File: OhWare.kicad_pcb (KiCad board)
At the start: 2 copper layers, 100 x 100 mm, 107 parts, among them J1 Screw_Terminal_01x03, J10 Conn_02x15_Odd_Even, J11 Conn_01x04_Pin, J12 Conn_01x03_Pin, J15 RJ45_Hanrun_HR911105A_Horizon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, J2 Conn_01x04_Pin, J4 Conn_01x02_Pin, J5 Conn_01x04_Pin, J6 Conn_01x02_Pin, J7 Conn_01x06_Pin, J8 Conn_01x04_Pin, J9 Conn_02x10_Odd_Even, SW1 SW_DIP_x01, SW2 SW_DIP_x01, SW3 SW_DIP_x01, U1 STM32F407VETx, U10 SP3485EN-L/TR, U2 SIT65HVD230DR, U3 SIT3490EESA, U4 XL1509-5.0E1, U5 AMS1117-3.3, U6 TL431M-0.3%-6AF, U7 LAN8720AI-CP-TR, U8 USB-TYPE-C-016, X1 X32258MOB4SI, X2 ABS07-32.768KHZ-T, X3 XL2EL89CSI-111YLC-25M

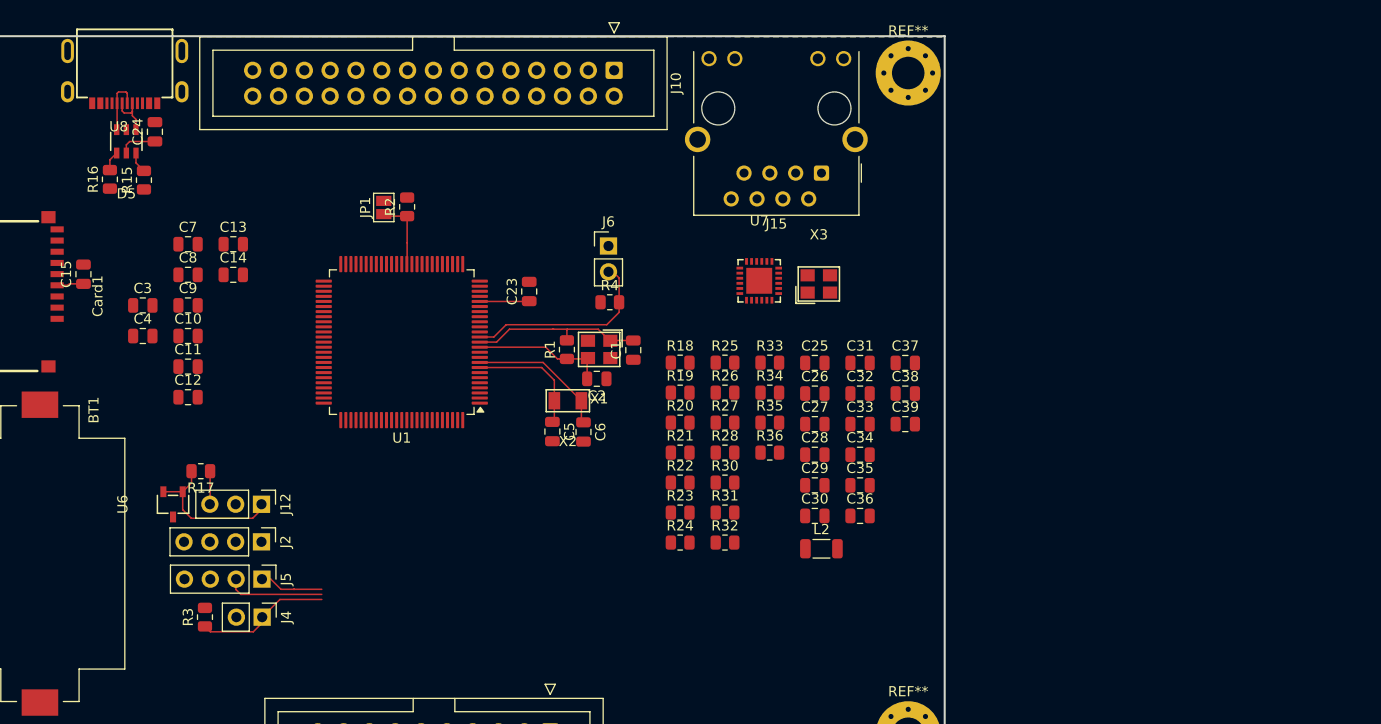
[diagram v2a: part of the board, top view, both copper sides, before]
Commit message: mcu circuit Done , + Ehernet Done (still placement is negotiable (best placement for minimal routing hustle))
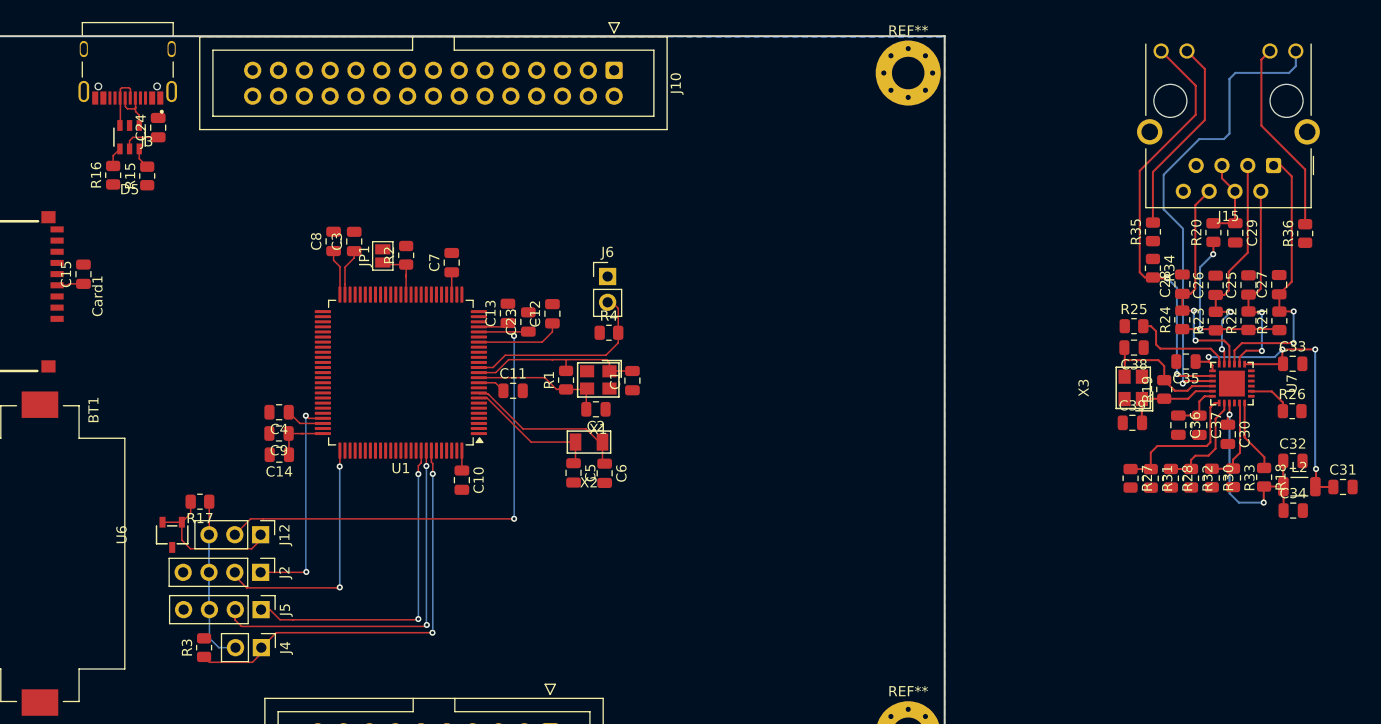
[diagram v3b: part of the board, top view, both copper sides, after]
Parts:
- removed U8: USB-TYPE-C-016, EasyEDA:USB-SMD_TYPE-C16PCB1.6073
- added J3: CQ-USB-C16PSMT01, EasyEDA:SHENZHEN-CHUANGQIN-TECHNOLOGY_CQ-USB-C16PSMT01, F.Cu at (119.6, 56.1)
- moved R21 60.4 mm to (232.9, 78.0), turned to 90 degrees
- moved R18 58.5 mm to (231.4, 93.4), turned to -90 degrees
- moved R22 58.1 mm to (229.9, 78.0), turned to 90 degrees
- moved R36 56.9 mm to (235.5, 69.4), turned to 90 degrees
- moved R23 56.0 mm to (226.7, 78.0), turned to 90 degrees
- moved R26 55.8 mm to (234.2, 86.9)
- moved R20 55.7 mm to (226.4, 69.3), turned to 90 degrees
- moved R24 54.0 mm to (223.4, 77.9), turned to 90 degrees
- moved C31 49.1 mm to (239.2, 94.4)
- moved C29 48.2 mm to (228.6, 69.4), turned to -90 degrees
- moved R30 47.9 mm to (226.3, 93.5), turned to -90 degrees
- moved C27 47.7 mm to (232.9, 74.5), turned to 90 degrees
- moved R19 47.6 mm to (221.6, 84.8), turned to 90 degrees
- moved U7 47.6 mm to (228.3, 84.2), turned to -90 degrees
- moved L2 47.4 mm to (234.9, 94.3)
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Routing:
- net +3V3: track 5.91 -> 70.1 mm, vias 0 -> 2
- net /Controller/VREF: track 4.88 -> 51.4 mm, vias 0 -> 2
- net /Ethernet/LED1/REGOFF: track 0.00 -> 46.4 mm, vias 0 -> 1
- net /Ethernet/LED2/nINTSEL: track 0.00 -> 41.8 mm, vias 0 -> 2
- net /Ethernet/VDDA: track 0.00 -> 34.1 mm, vias 0 -> 4
- net /Controller/BOOT0: track 13.4 -> 42.2 mm, vias 0 -> 2
- net /Ethernet/TXP: track 0.00 -> 28.1 mm, vias 0 -> 2
- net /Controller/UART1_Rx: track 9.94 -> 37.6 mm, vias 0 -> 2
- net /Controller/UART1_Tx: track 6.36 -> 32.7 mm, vias 0 -> 2
- net /Controller/SWCLK (PA14): track 0.00 -> 24.7 mm, vias 0 -> 2
- net /Ethernet/RXP: track 0.00 -> 23.3 mm, vias 0 -> 2
- net /Ethernet/RXN: track 0.00 -> 22.8 mm, vias 0 -> 2
- net /Controller/SWDIO (PA13): track 0.00 -> 21.7 mm, vias 0 -> 2
- net /Ethernet/TXN: track 0.00 -> 21.0 mm, vias 0 -> 2
- net Net-(J15-Pad11): track 0.00 -> 19.7 mm
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
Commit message: Added Base
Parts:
- removed BT1: CR2032, Battery:BatteryHolder_Keystone_1060_1x2032
- removed C10, C11, C12, C13, C15, C23, C24, C7, C8, C9: 100n, Capacitor_SMD:C_0805_2012Metric
- removed C14, C31, C32: 4.7u, Capacitor_SMD:C_0805_2012Metric
- removed C25, C26, C27, C28: 10pF, Capacitor_SMD:C_0805_2012Metric
- removed C29: 22nF, Capacitor_SMD:C_0805_2012Metric
- removed C3, C4: 2.2u, Capacitor_SMD:C_0805_2012Metric
- removed C30, C33, C34, C35, C37: 0.1uF, Capacitor_SMD:C_0805_2012Metric
- removed C36: 1uF, Capacitor_SMD:C_0805_2012Metric
- removed C38, C39: 30pF, Capacitor_SMD:C_0805_2012Metric
- removed C5, C6: 12.5pF, Capacitor_SMD:C_0805_2012Metric
- removed Card1: TF-01A, EasyEDA:TF-SMD_TF-01A
- removed D5: USBLC6-2SC6, EasyEDA:SOT-23-6_L2.9-W1.6-P0.95-LS2.8-BL
- removed J12: Conn_01x03_Pin, Connector_PinHeader_2.54mm:PinHeader_1x03_P2.54mm_Vertical
- removed J15: RJ45_Hanrun_HR911105A_Horizontal, EasyEDA:RJ45_Hanrun_HR911105A_Horizontal
- removed J2, J5: Conn_01x04_Pin, Connector_PinHeader_2.54mm:PinHeader_1x04_P2.54mm_Vertical
- removed J3: CQ-USB-C16PSMT01, EasyEDA:SHENZHEN-CHUANGQIN-TECHNOLOGY_CQ-USB-C16PSMT01
- removed J4, J6: Conn_01x02_Pin, Connector_PinHeader_2.54mm:PinHeader_1x02_P2.54mm_Vertical
- removed JP1: Jumper_2_Open, Jumper:SolderJumper-2_P1.3mm_Open_Pad1.0x1.5mm
- removed L2: 2A/0.05, Inductor_SMD:L_1206_3216Metric
- removed R1, R2, R3, R4: 10K, Resistor_SMD:R_0805_2012Metric
- removed R15, R16, R20: 0, Resistor_SMD:R_0805_2012Metric
- removed R17: 1k, Resistor_SMD:R_0805_2012Metric
- removed R18: 1.5k-1%, Resistor_SMD:R_0805_2012Metric
- removed R19: 1M, Resistor_SMD:R_0805_2012Metric
- removed R21, R22, R23, R24: 49.9-1%, Resistor_SMD:R_0805_2012Metric
- removed R25: 12.1k-1%, Resistor_SMD:R_0805_2012Metric
- removed R26: 33, Resistor_SMD:R_0805_2012Metric
- removed R27, R28, R30: 10, Resistor_SMD:R_0805_2012Metric
- removed R31, R32, R33: 4.7k, Resistor_SMD:R_0805_2012Metric
- removed R34: 10k, Resistor_SMD:R_0805_2012Metric
- removed R35, R36: 470, Resistor_SMD:R_0805_2012Metric
- removed X1: X32258MOB4SI, EasyEDA:CRYSTAL-SMD_4P-L3.2-W2.5-BL
- removed X2: ABS07-32.768KHZ-T, EasyEDA:OSC-SMD_2P-L3.2-W1.5
- removed X3: XL2EL89CSI-111YLC-25M, EasyEDA:CRYSTAL-SMD_4P-L3.2-W2.5-BL
- C1, C2: value 20p -> 10u; footprint Capacitor_SMD:C_0805_2012Metric -> Capacitor_SMD:C_1206_3216Metric_Pad1.33x1.80mm_HandSolder
- U1: value STM32F407VETx -> ~; footprint Package_QFP:LQFP-100_14x14mm_P0.5mm -> libMain:WeAct_STM32F12
- U6: value TL431M-0.3%-6AF -> AMS1117-3.3; footprint EasyEDA:SOT-23-3_L2.9-W1.6-P1.90-LS2.8-BR -> Package_TO_SOT_SMD:SOT-223-3_TabPin2
- U7: value LAN8720AI-CP-TR -> ESP32-WROOM-32; footprint EasyEDA:QFN-24_L4.0-W4.0-P0.50-BL-EP2.6 -> EasyEDA:WIFIM-SMD_ESP32-WROOM-32-N4
- moved U7 111.7 mm to (116.6, 84.5), turned to 90 degrees
- moved C1 66.3 mm to (107.7, 108.4), turned to 0 degrees
- moved C2 56.4 mm to (110.4, 98.1), turned to 0 degrees
- moved U1 31.4 mm to (177.8, 85.4), turned to 90 degrees
- moved U6 15.3 mm to (109.3, 103.1), turned to 0 degrees
- moved J1 1.51 mm to (103.1, 141.8)
- moved C17 1.51 mm to (191.9, 132.0)
- moved D4 1.51 mm to (130.2, 141.8)
- moved J8 1.51 mm to (163.2, 145.3)
- moved SW2 1.51 mm to (163.7, 134.8), turned to 90 degrees
- moved U10 1.51 mm to (169.7, 133.4)
- moved U2 1.51 mm to (155.2, 135.3)
- moved C16 1.51 mm to (155.2, 130.2)
- moved J11 1.51 mm to (177.5, 145.3)
- moved L1 1.51 mm to (137.4, 139.6)
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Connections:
- C1 pad 1: GND -> +5V
- C1 pad 2: Net-(U1-PH1) -> GND
- C2 pad 1: GND -> +3.3VESP
- C2 pad 2: Net-(U1-PH0) -> GND
- J9 pad 1: /Controller/SPI1_MOSI -> /SPI_I2C_UART_expansion/SPI1_MOSI
- J9 pad 10: /Controller/UART3_Rx -> /SPI_I2C_UART_expansion/UART3_Rx
- J9 pad 11: /Controller/UART6_Tx -> /SPI_I2C_UART_expansion/UART6_Tx
- J9 pad 12: /Controller/UART6_Rx -> /SPI_I2C_UART_expansion/UART6_Rx
- J9 pad 13: /Controller/I2C1_SDA -> /SPI_I2C_UART_expansion/I2C1_SDA
- J9 pad 14: /Controller/I2C1_SCL -> /SPI_I2C_UART_expansion/I2C1_SCL
- J9 pad 2: /Controller/SPI1_MISO -> /SPI_I2C_UART_expansion/SPI1_MISO
- J9 pad 3: /Controller/SPI1_SCK -> /SPI_I2C_UART_expansion/SPI1_CLK
- J9 pad 4: /Controller/SPI1_CS1 -> /SPI_I2C_UART_expansion/SPI1_CS1
- J9 pad 5: /Controller/SPI1_CS2 -> /SPI_I2C_UART_expansion/SPI1_CS2
- J9 pad 9: /Controller/UART3_Tx -> /SPI_I2C_UART_expansion/UART3_Tx
- SW2 pad 1: Net-(R9-Pad1) -> /CAN/CAN_H
- SW2 pad 2: /CAN/CAN_H -> Net-(R9-Pad1)
- U1 pad 10: GND -> unconnected-(U1-C3-Pad10)
- U1 pad 11: +3V3 -> unconnected-(U1-A2-Pad11)
- U1 pad 12: Net-(U1-PH0) -> unconnected-(U1-A1-Pad12)
- U1 pad 13: Net-(U1-PH1) -> unconnected-(U1-A4-Pad13)
- U1 pad 14: /Controller/NRST -> unconnected-(U1-A3-Pad14)
- U1 pad 16: /Controller/ETH_MDC -> unconnected-(U1-A5-Pad16)
- U1 pad 19: +3V3 -> unconnected-(U1-B0-Pad19)
- U1 pad 2: unconnected-(U1-PE3-Pad2) -> GND
- U1 pad 20: GND -> unconnected-(U1-C5-Pad20)
- U1 pad 21: /Controller/VREF -> unconnected-(U1-B2-Pad21)
- U1 pad 22: +3V3 -> unconnected-(U1-B1-Pad22)
- U1 pad 24: /Controller/ETH_REFCLK -> unconnected-(U1-B10-Pad24)
- U1 pad 25: /Controller/ETH_MDIO -> unconnected-(U1-3.3-Pad25)
- U1 pad 26: unconnected-(U1-PA3-Pad26) -> GND
- U1 pad 27: GND -> unconnected-(U1-3.3-Pad27)
- U1 pad 28: +3V3 -> GND
- U1 pad 30: unconnected-(U1-PA5-Pad30) -> GND
- U1 pad 32: /Controller/ETH_CRSDV -> GND
- U1 pad 33: /Controller/ETH_RMII_RXD0 -> unconnected-(U1-B7-Pad33)
- U1 pad 34: /Controller/ETH_RMII_RXD1 -> unconnected-(U1-B8-Pad34)
- U1 pad 37: /Controller/BOOT1 -> unconnected-(U1-B3-Pad37)
- U1 pad 39: /Controller/TIM1_CH1N -> unconnected-(U1-C12-Pad39)
- U1 pad 40: /Controller/TIM1_CH1 -> unconnected-(U1-D2-Pad40)
- U1 pad 41: /Controller/TIM1_CH2N -> unconnected-(U1-C10-Pad41)
- U1 pad 42: /Controller/TIM1_CH2 -> unconnected-(U1-C11-Pad42)
- U1 pad 43: /Controller/TIM1_CH3N -> unconnected-(U1-A12-Pad43)
- U1 pad 44: /Controller/TIM1_CH3 -> unconnected-(U1-A15-Pad44)
- U1 pad 45: /Controller/SPI1_CS1 -> unconnected-(U1-A10-Pad45)
- U1 pad 46: /Controller/SPI1_CS2 -> unconnected-(U1-A11-Pad46)
- U1 pad 48: /Controller/ETH_RMII_TXEN -> unconnected-(U1-A9-Pad48)
- U1 pad 49: Net-(U1-VCAP_1) -> unconnected-(U1-C8-Pad49)
- U1 pad 50: +3V3 -> unconnected-(U1-C9-Pad50)
- U1 pad 51: /Controller/ETH_RMII_TXD0 -> unconnected-(U1-C6-Pad51)
- U1 pad 52: /Controller/ETH_RMII_TXD1 -> unconnected-(U1-C7-Pad52)
- U1 pad 55: /Controller/UART3_Tx -> unconnected-(U1-B12-Pad55)
- U1 pad 56: /Controller/UART3_Rx -> unconnected-(U1-B13-Pad56)
- U1 pad 59: unconnected-(U1-PD12-Pad59) -> GND
- U1 pad 6: Net-(BT1-+) -> unconnected-(U1-C15-Pad6)
- U1 pad 60: unconnected-(U1-PD13-Pad60) -> GND
- U1 pad 7: /Controller/ETH_nRST -> unconnected-(U1-C2-Pad7)
- U1 pad 8: Net-(U1-PC14) -> unconnected-(U1-C1-Pad8)
- U1 pad 9: Net-(U1-PC15) -> unconnected-(U1-A0-Pad9)
- U10 pad 1: /Controller/UART2_Rx -> /RS485/RO
- U10 pad 4: /Controller/UART2_Tx -> /RS485/DI
- U3 pad 2: /Controller/UART2_Rx -> /RS485/RO
- U3 pad 3: /Controller/UART2_Tx -> /RS485/DI
- U6 pad 1: /Controller/VREF_2.5V -> GND
- U6 pad 2: /Controller/VREF_2.5V -> +3.3VESP
- U6 pad 3: GND -> +5V
- U7 pad 1: /Ethernet/VDDA -> GND
- U7 pad 11: /Ethernet/MODE2 -> unconnected-(U7-IO26-Pad11)
- U7 pad 12: /Controller/ETH_MDIO -> unconnected-(U7-IO27-Pad12)
- U7 pad 13: /Controller/ETH_MDC -> unconnected-(U7-IO14-Pad13)
- U7 pad 14: Net-(U7-nINT/REFCLKO) -> unconnected-(U7-IO12-Pad14)
- U7 pad 15: /Controller/ETH_nRST -> GND
- U7 pad 16: /Controller/ETH_RMII_TXEN -> unconnected-(U7-IO13-Pad16)
- U7 pad 17: /Controller/ETH_RMII_TXD0 -> unconnected-(U7-SHD/SD2-Pad17)
- U7 pad 18: /Controller/ETH_RMII_TXD1 -> unconnected-(U7-SWP/SD3-Pad18)
- U7 pad 19: /Ethernet/VDDA -> unconnected-(U7-SCS/CMD-Pad19)
- U7 pad 2: /Ethernet/LED2/nINTSEL -> +3.3VESP
- U7 pad 20: /Ethernet/TXN -> unconnected-(U7-SCK/CLK-Pad20)
- U7 pad 21: /Ethernet/TXP -> unconnected-(U7-SDO/SD0-Pad21)
- U7 pad 22: /Ethernet/RXN -> unconnected-(U7-SDI/SD1-Pad22)
- U7 pad 23: /Ethernet/RXP -> unconnected-(U7-IO15-Pad23)
- U7 pad 24: Net-(U7-RBIAS) -> unconnected-(U7-IO2-Pad24)
- U7 pad 25: GND -> Net-(U7-IO0)
- U7 pad 3: /Ethernet/LED1/REGOFF -> /Esp32/RST
- U7 pad 4: /Ethernet/XTAL2 -> unconnected-(U7-SENSOR_VP-Pad4)
- U7 pad 5: /Ethernet/XTAL1 -> unconnected-(U7-SENSOR_VN-Pad5)
- U7 pad 6: /Ethernet/VDDCR -> unconnected-(U7-IO34-Pad6)
- U7 pad 7: /Ethernet/MODE1 -> unconnected-(U7-IO35-Pad7)
- U7 pad 8: /Ethernet/MODE0 -> unconnected-(U7-IO32-Pad8)
- U7 pad 9: +3V3 -> unconnected-(U7-IO33-Pad9)
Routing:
- net +3V3: track 70.1 -> 0.00 mm, vias 2 -> 0
- net +3.3V: track 22.5 -> 92.5 mm, vias 0 -> 2
- net GND: track 75.7 -> 143.1 mm, vias 24 -> 29
- net /Controller/VREF: track 51.4 -> 0.00 mm, vias 2 -> 0
- net /Ethernet/LED1/REGOFF: track 46.4 -> 0.00 mm, vias 1 -> 0
- net /Controller/BOOT0: track 42.2 -> 0.00 mm, vias 2 -> 0
- net /Ethernet/LED2/nINTSEL: track 41.8 -> 0.00 mm, vias 2 -> 0
- net /Controller/UART1_Rx: track 37.6 -> 0.00 mm, vias 2 -> 0
- net /Ethernet/VDDA: track 34.1 -> 0.00 mm, vias 4 -> 0
- net /Controller/UART1_Tx: track 32.7 -> 0.00 mm, vias 2 -> 0
- net /Ethernet/TXP: track 28.1 -> 0.00 mm, vias 2 -> 0
- net /RS485/RO: track 0.00 -> 25.4 mm, vias 0 -> 2
- net /RS485/DI: track 0.00 -> 24.8 mm
- net /Controller/SWCLK (PA14): track 24.7 -> 0.00 mm, vias 2 -> 0
- net /Ethernet/RXP: track 23.3 -> 0.00 mm, vias 2 -> 0
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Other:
- board size 100 x 100 mm -> 100 x 105.4 mm

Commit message: UPDATED
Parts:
- added C3: 0.1u, Capacitor_SMD:C_1206_3216Metric_Pad1.33x1.80mm_HandSolder, F.Cu at (116.2, 95.7)
- added D1: LED, LED_SMD:LED_1206_3216Metric_Pad1.42x1.75mm_HandSolder, F.Cu at (122.0, 103.2)
- added D2: LED, LED_SMD:LED_1206_3216Metric_Pad1.42x1.75mm_HandSolder, F.Cu at (126.3, 103.2)
- added D5: LED, LED_SMD:LED_1206_3216Metric_Pad1.42x1.75mm_HandSolder, F.Cu at (117.2, 103.2)
- added J2: Conn_01x03_Pin, Connector_PinHeader_2.54mm:PinHeader_1x03_P2.54mm_Horizontal, F.Cu at (108.8, 64.9)
- added J3: Conn_01x02_Pin, Connector_PinHeader_2.54mm:PinHeader_1x02_P2.54mm_Horizontal, F.Cu at (121.4, 64.8)
- added J4: Conn_01x03_Pin, Connector_PinHeader_2.54mm:PinHeader_1x03_P2.54mm_Horizontal, F.Cu at (112.4, 64.8)
- added R1: 10k, Resistor_SMD:R_1206_3216Metric_Pad1.30x1.75mm_HandSolder, F.Cu at (110.7, 94.1)
- added R2: 470, Resistor_SMD:R_1206_3216Metric_Pad1.30x1.75mm_HandSolder, F.Cu at (120.3, 95.5)
- added R3: 1k, Resistor_SMD:R_1206_3216Metric_Pad1.30x1.75mm_HandSolder, F.Cu at (126.3, 108.6)
- added R4: 1k, Resistor_SMD:R_1206_3216Metric_Pad1.30x1.75mm_HandSolder, F.Cu at (122.0, 108.5)
- added R5: 1k, Resistor_SMD:R_1206_3216Metric_Pad1.30x1.75mm_HandSolder, F.Cu at (117.3, 108.5)
- C16, C17, C40: footprint Capacitor_SMD:C_0805_2012Metric -> Capacitor_SMD:C_1206_3216Metric_Pad1.33x1.80mm_HandSolder
- J1: moved to B.Cu
- J11, J8: footprint Connector_JST:JST_XH_B4B-XH-A_1x04_P2.50mm_Vertical -> Connector_JST:JST_XH_S4B-XH-A_1x04_P2.50mm_Horizontal; moved to B.Cu
- J7: footprint Connector_JST:JST_XH_B6B-XH-A_1x06_P2.50mm_Vertical -> Connector_JST:JST_XH_S6B-XH-A_1x06_P2.50mm_Horizontal; moved to B.Cu
- R8: footprint Resistor_SMD:R_0805_2012Metric -> Resistor_SMD:R_1206_3216Metric_Pad1.30x1.75mm_HandSolder
- moved J1 10.1 mm to (113.1, 141.8), turned to 180 degrees
- moved U7 4.44 mm to (116.9, 80.0)
- moved C2 1.38 mm to (110.7, 96.7)
- moved U6 1.38 mm to (109.5, 101.8)
- moved C1 1.38 mm to (107.9, 107.0)
- moved R8 0.62 mm to (158.9, 139.9)
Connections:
- J1 pad 1: Earth -> +12V
- J1 pad 3: +12V -> Earth
- U1 pad 1: unconnected-(U1-VB-Pad1) -> +3.3V
- U1 pad 25: unconnected-(U1-3.3-Pad25) -> +3.3V
- U1 pad 27: unconnected-(U1-3.3-Pad27) -> +3.3V
- U1 pad 29: unconnected-(U1-3.3-Pad29) -> +3.3V
- U7 pad 10: unconnected-(U7-IO25-Pad10) -> /Esp32/INDESP_LED0
- U7 pad 11: unconnected-(U7-IO26-Pad11) -> /Esp32/INDESP_LED1
- U7 pad 12: unconnected-(U7-IO27-Pad12) -> /Esp32/INDESP_LED2
- U7 pad 13: unconnected-(U7-IO14-Pad13) -> /Esp32/SPI_CLK
- U7 pad 14: unconnected-(U7-IO12-Pad14) -> /Esp32/SPI_MISO
- U7 pad 16: unconnected-(U7-IO13-Pad16) -> /Esp32/SPI_MOSI
- U7 pad 23: unconnected-(U7-IO15-Pad23) -> /Esp32/SPI_CS
- U7 pad 27: unconnected-(U7-IO16-Pad27) -> Net-(J4-Pin_2)
- U7 pad 28: unconnected-(U7-IO17-Pad28) -> Net-(J4-Pin_1)
- U7 pad 3: /Esp32/RST -> Net-(U7-EN)
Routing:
- net +3.3V: track 92.5 -> 163.4 mm, vias 2 -> 7
- net +5V: track 33.5 -> 85.3 mm, vias 1 -> 3
- net +3.3VESP: track 16.0 -> 41.1 mm, vias 0 -> 2
- net /Esp32/INDESP_LED2: track 0.00 -> 16.3 mm, vias 0 -> 2
- net Net-(J2-Pin_2): track 0.00 -> 14.3 mm
- net /Esp32/INDESP_LED0: track 0.00 -> 14.1 mm, vias 0 -> 2
- net /Esp32/INDESP_LED1: track 0.00 -> 13.3 mm, vias 0 -> 2
- net Net-(U7-EN): track 0.00 -> 12.9 mm
- net Net-(J4-Pin_1): track 0.00 -> 12.3 mm
- net Net-(J4-Pin_2): track 0.00 -> 11.7 mm
- net Net-(J2-Pin_1): track 0.00 -> 9.16 mm
- net Net-(J3-Pin_1): track 0.00 -> 7.48 mm
- net Net-(D5-A): track 0.00 -> 2.31 mm
- net Net-(D2-A): track 0.00 -> 2.30 mm
- net Net-(D1-A): track 0.00 -> 2.29 mm
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
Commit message: Latest Changes
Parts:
- added D3: LED, LED_SMD:LED_1206_3216Metric_Pad1.42x1.75mm_HandSolder, F.Cu at (65.7, 78.8)
- added D6: LED, LED_SMD:LED_1206_3216Metric_Pad1.42x1.75mm_HandSolder, F.Cu at (72.4, 79.0)
- added D7: LED, LED_SMD:LED_1206_3216Metric_Pad1.42x1.75mm_HandSolder, F.Cu at (78.8, 79.0)
- added JP1: Jumper_2_Bridged, Jumper:Jumper_Harwin_S1621_P10.9mm, B.Cu at (146.9, 71.6)
- added R10: 1k, Resistor_SMD:R_1206_3216Metric_Pad1.30x1.75mm_HandSolder, F.Cu at (74.9, 79.0)
- added R11: 1k, Resistor_SMD:R_1206_3216Metric_Pad1.30x1.75mm_HandSolder, F.Cu at (81.3, 79.1)
- added R7: 1k, Resistor_SMD:R_1206_3216Metric_Pad1.30x1.75mm_HandSolder, F.Cu at (68.2, 79.0)
- added SW4: SW_Push, Button_Switch_SMD:SW_SPST_CK_RS282G05A3, F.Cu at (51.3, 103.0)
- moved REF** 66.5 mm to (129.9, 52.4)
- moved REF** 66.5 mm to (129.9, 117.4)
- moved C18 66.4 mm to (55.0, 144.9)
- moved J8 66.4 mm to (96.9, 150.6)
- moved R14 66.4 mm to (126.4, 141.7)
- moved R6 66.4 mm to (108.0, 139.0)
- moved SW2 66.4 mm to (97.5, 140.2)
- moved U10 66.4 mm to (103.5, 138.7)
- moved U2 66.4 mm to (89.0, 140.7)
- moved C16 66.4 mm to (89.0, 135.6)
- moved C19 66.4 mm to (60.7, 148.0)
- moved C20 66.4 mm to (79.1, 145.0)
- moved C21 66.4 mm to (82.7, 141.2)
- moved C22 66.4 mm to (71.8, 134.8)
- moved C40 66.4 mm to (104.6, 144.2)
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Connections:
- net /Esp32/SPI_CLK renamed /Controller/SPI3_SCK
- net /Esp32/SPI_MOSI renamed /Controller/SPI3_MOSI
- R2 pad 1: /Esp32/EN -> /Controller/SPI3_DEN
- U1 pad 23: unconnected-(U1-B11-Pad23) -> /Controller/USART3_RX
- U1 pad 24: unconnected-(U1-B10-Pad24) -> /Controller/USART3_TX
- U1 pad 31: unconnected-(U1-B9-Pad31) -> /CAN/CAN_TXD
- U1 pad 34: unconnected-(U1-B8-Pad34) -> /CAN/CAN_RXD
- U1 pad 4: unconnected-(U1-C13-Pad4) -> /Controller/SPI3_DEN
- U10 pad 1: /RS485/RO -> /Controller/USART3_RX
- U10 pad 4: /RS485/DI -> /Controller/USART3_TX
- U3 pad 2: /RS485/RO -> /Controller/USART3_RX
- U3 pad 3: /RS485/DI -> /Controller/USART3_TX
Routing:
- net /CAN/CAN_RXD: track 0.00 -> 117.4 mm, vias 0 -> 7
- net /CAN/CAN_TXD: track 0.00 -> 102.0 mm, vias 0 -> 6
- net /Controller/USART3_TX: track 0.00 -> 90.1 mm, vias 0 -> 3
- net +3.3V: track 163.4 -> 228.6 mm, vias 7 -> 9
- net /Controller/USART3_RX: track 0.00 -> 59.8 mm, vias 0 -> 4
- net /Controller/SPI3_DEN: track 0.00 -> 45.7 mm, vias 0 -> 1
- net GND: track 144.4 -> 177.7 mm, vias 30 -> 34
- net /RS485/RO: track 25.5 -> 0.00 mm, vias 2 -> 0
- net /RS485/DI: track 24.8 -> 0.00 mm
- net +5V: track 85.3 -> 91.8 mm
- net Net-(U7-EN): track 12.9 -> 18.1 mm
- net +3.3VESP: track 41.1 -> 45.4 mm
- net /Esp32/INDESP_LED2: track 16.3 -> 20.3 mm
- net /Esp32/INDESP_LED1: track 13.3 -> 17.0 mm
- net Net-(D3-A): track 0.00 -> 2.53 mm
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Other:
- board size 100 x 105.4 mm -> 100 x 114.7 mm
